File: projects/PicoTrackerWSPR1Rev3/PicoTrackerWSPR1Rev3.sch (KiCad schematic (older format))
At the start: 54 parts, among them J1 Conn_01x02, M1 SIP32431DR3-T1GE3, M2 SIP32431DR3-T1GE3, M3 UBLOX_NEO-6, M4 SI5351A, U1 ATMEGA328P-AU, Y1 CRYSTAL_ABM8G

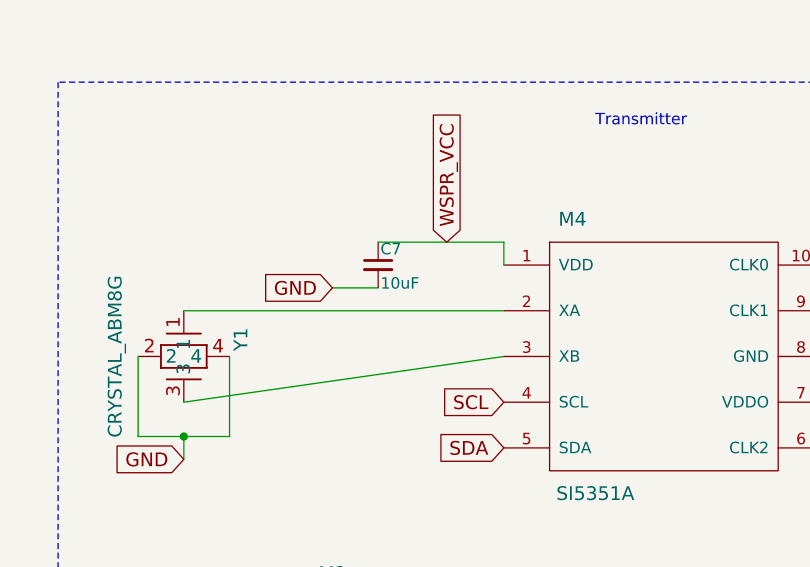
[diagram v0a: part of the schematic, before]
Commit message: KiCad PicoTrackerWSPR1Rev3 updated cap value on CLKGEN power input from 10uF to .1uF
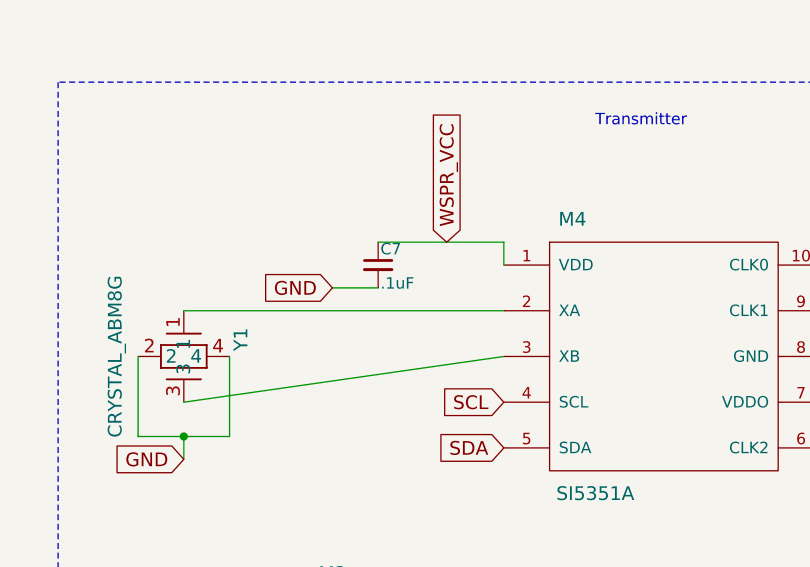
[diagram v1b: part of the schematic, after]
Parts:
- C7: value 10uF -> .1uF
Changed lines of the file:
@@
 P 13000 7050
 F 0 "C7" H 13010 7120 50  0000 L CNN
-F 1 "10uF" H 13010 6970 50  0000 L CNN
+F 1 ".1uF" H 13010 6970 50  0000 L CNN
 F 2 "Capacitors_SMD:C_0603_HandSoldering" H 13000 7050 50  0001 C CNN
 F 3 "" H 13000 7050 50  0001 C CNN
